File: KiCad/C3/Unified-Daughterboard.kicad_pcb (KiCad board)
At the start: 2 copper layers, 18 x 16.5 mm, 17 parts, among them IC1 NCP380LSN05AAT1G, J1 TYPE-C-31-M12_13, J2 SM04B-SRSS-TB(LF)(SN), J3 Conn_02x02_Odd_Even, U1 TPD4E05U06DQAR

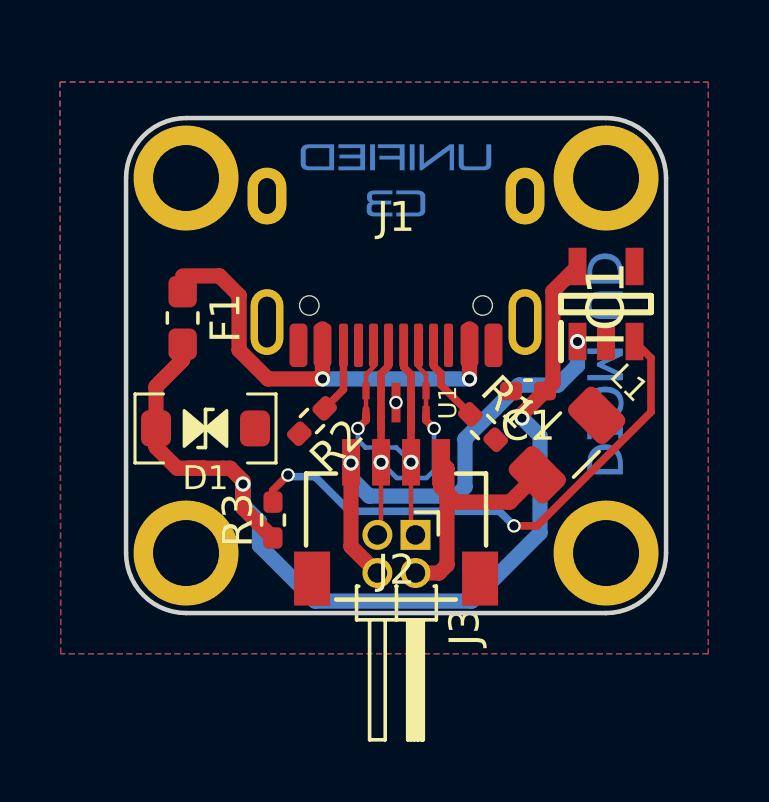
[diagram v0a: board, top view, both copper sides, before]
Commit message: change back and add decoupling cap
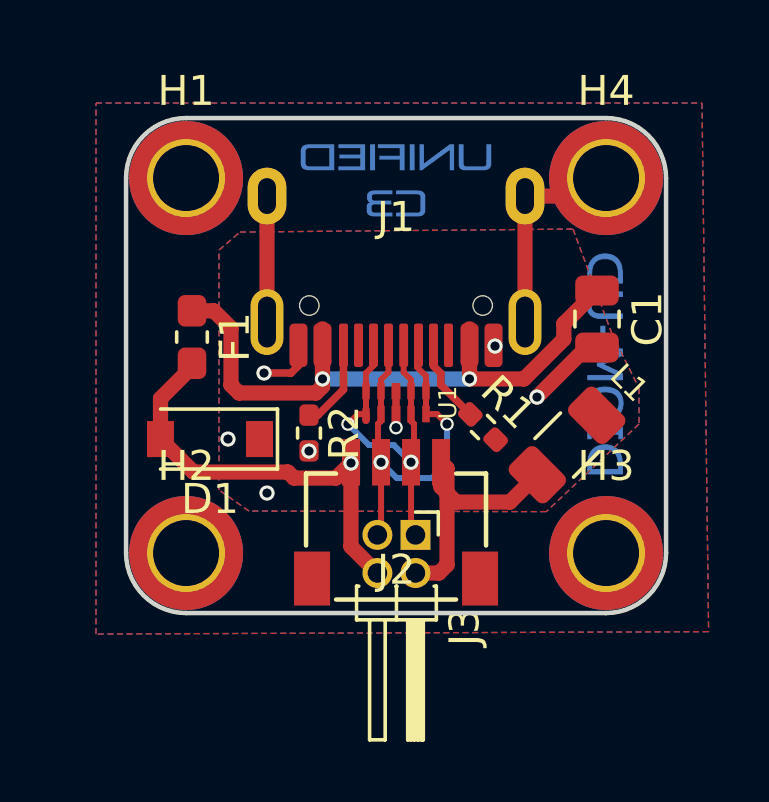
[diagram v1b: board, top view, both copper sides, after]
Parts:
- removed IC1: NCP380LSN05AAT1G, SamacSys_Parts:SOT95P275X110-5N
- removed MH1, MH2, MH3, MH4: Mount-M2, random-keyboard-parts:Generic-Mounthole
- removed R3: 100k, Resistor_SMD:R_0402_1005Metric_Pad0.72x0.64mm_HandSolder
- added H1: MountingHole_Pad, MountingHole:MountingHole_2.2mm_M2_DIN965_Pad_TopBottom, F.Cu at (68.0, 58.5)
- added H2: MountingHole_Pad, MountingHole:MountingHole_2.2mm_M2_DIN965_Pad_TopBottom, F.Cu at (68.0, 71.0)
- added H3: MountingHole_Pad, MountingHole:MountingHole_2.2mm_M2_DIN965_Pad_TopBottom, F.Cu at (82.0, 71.0)
- added H4: MountingHole_Pad, MountingHole:MountingHole_2.2mm_M2_DIN965_Pad_TopBottom, F.Cu at (82.0, 58.5)
- C1: value 1u -> 10u; footprint Capacitor_SMD:C_0402_1005Metric_Pad0.74x0.62mm_HandSolder -> Capacitor_SMD:C_0805_2012Metric
- D1: footprint acheron_Components:D_SOD-123_Bidirectional -> Diode_SMD:D_SOD-123
- moved C1 3.32 mm to (81.7, 63.2), turned to -90 degrees
- moved F1 0.71 mm to (68.2, 63.8)
- moved R2 0.41 mm to (72.1, 67.0), turned to -90 degrees
- moved D1 0.38 mm to (68.8, 67.2)
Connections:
- C1 pad 1: VCC -> VBUS
- C1 pad 2: GNDPWR -> GNDREF
- D1 pad 1: GNDPWR -> GNDREF
- J1 pad A1: GNDPWR -> GNDREF
- J1 pad B1: GNDPWR -> GNDREF
- J2 pad 1: VCCQ -> VCC
- J3 pad 4: VCCQ -> VCC
- L1 pad 2: GNDPWR -> GNDREF
- R1 pad 2: GNDPWR -> GNDREF
- R2 pad 2: GNDPWR -> GNDREF
- U1 pad 3: GNDPWR -> GNDREF
- U1 pad 8: GNDPWR -> GNDREF
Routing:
- net VCC: track 33.8 -> 14.1 mm, vias 2 -> 1
- net Net-(IC1-Pad3): track 18.5 -> 0.00 mm, vias 2 -> 0
- net VCCQ: track 16.1 -> 0.00 mm, vias 2 -> 0
- net GNDPWR: track 0.17 -> 11.6 mm, vias 1 -> 0
- net GNDREF: track 0.00 -> 6.63 mm, vias 0 -> 7
- net VBUS: track 15.4 -> 21.0 mm
- net DA+: track 16.1 -> 13.9 mm
- net DA-: track 15.9 -> 14.9 mm
- net Net-(J1-PadB5): track 2.91 -> 3.53 mm
- added copper zone on B.Cu, net GNDREF
- added copper zone on F.Cu, net GNDREF
